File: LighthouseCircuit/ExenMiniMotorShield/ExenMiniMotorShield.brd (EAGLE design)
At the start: 15.2 x 6.3 mm, 13 parts, among them J3 SM02B-SRSS, Q1 DMP2035U

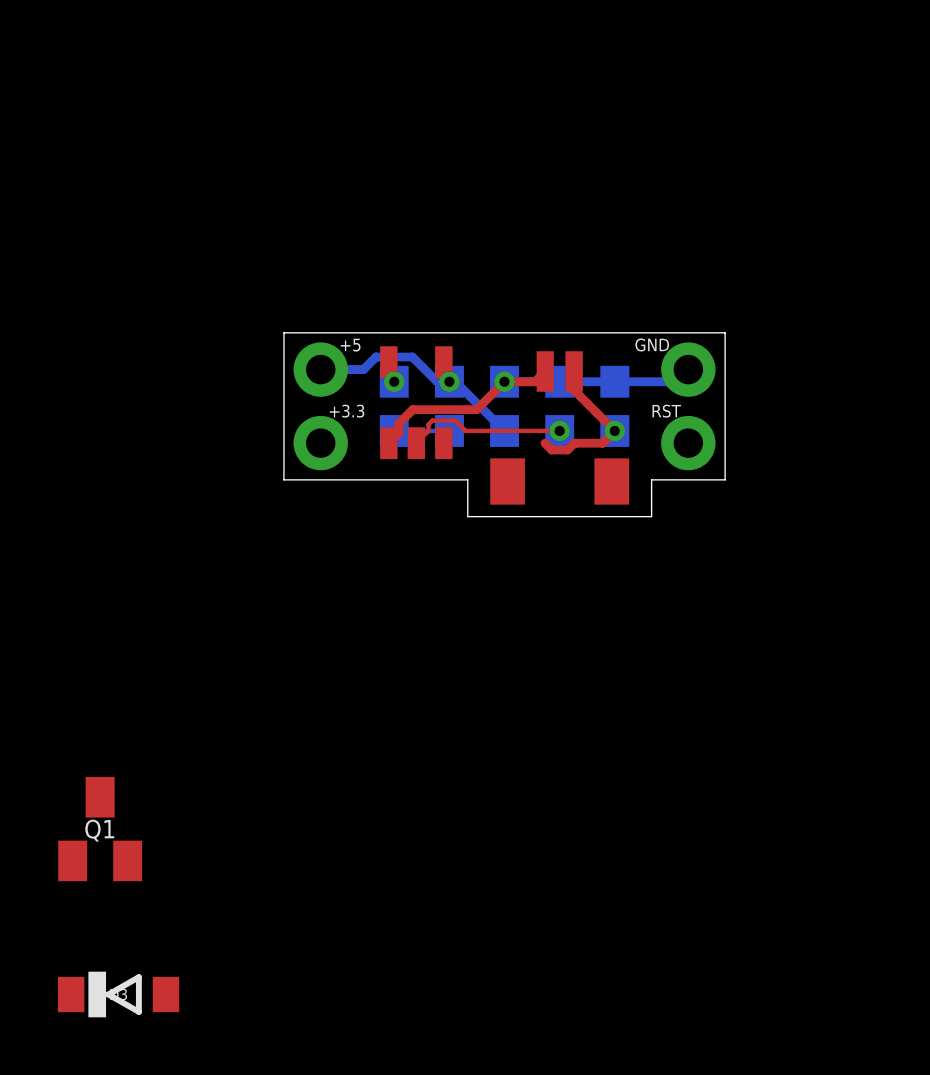
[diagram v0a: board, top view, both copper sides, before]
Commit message: Moved to separate PID configuration for each wheel. Since the left wheel is offset toward the rear and the right wheel is offset toward the front, the left wheel needs to be less aggressive or the Zippy will turn more quickly to the right and will tilt the robot and pull the right wheel off the ground, preventing contact with the floor. On the other hand, the right wheel needs to be more aggressive or turns to the left will be slower than turns to the right.
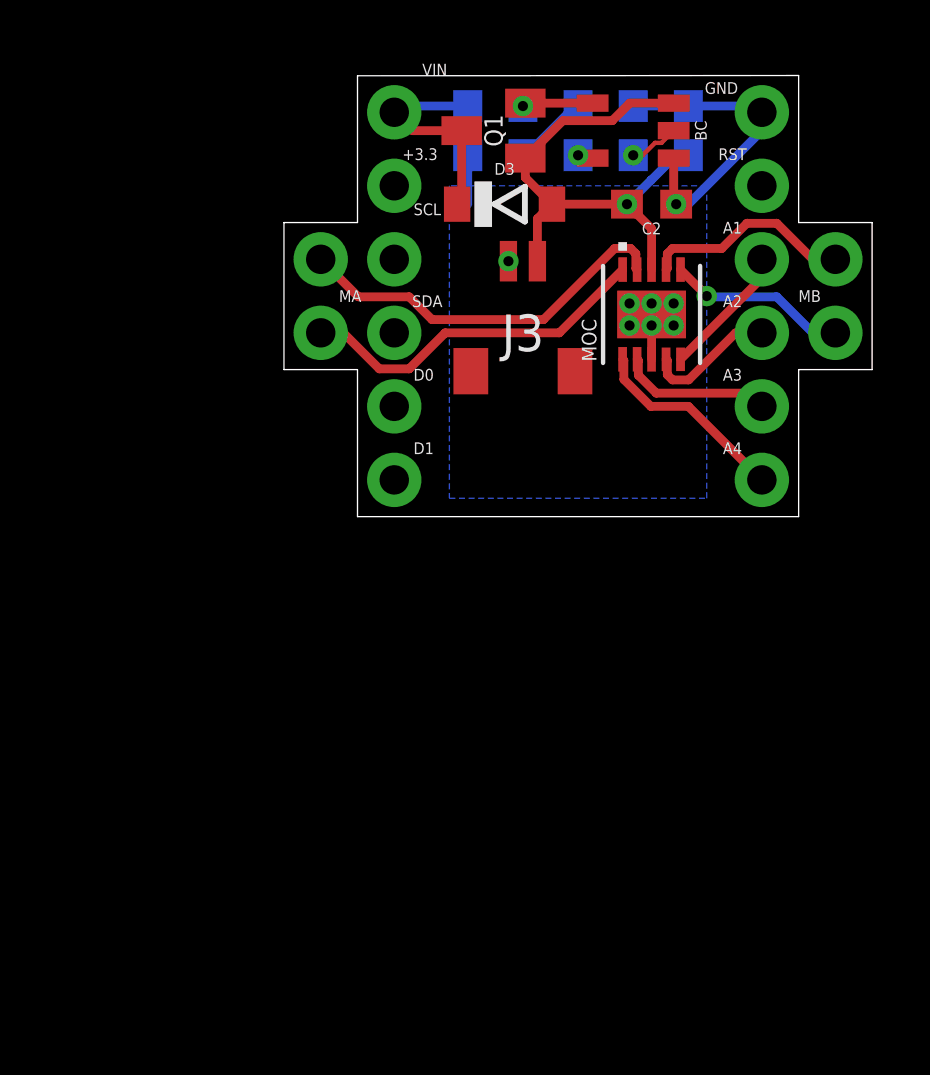
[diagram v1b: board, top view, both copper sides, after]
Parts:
- removed +5: (no value), SparkFun-Connectors:1X01_NO_SILK
- added A1, A2, A3, A4, D0, D1, MA01, MA02, MB01, MBO2, SCL, SDA, VIN: (no value), SparkFun-Connectors:1X01_NO_SILK
- added CB: 10μF, SparkFun-Capacitors:0603
- added MOC: A3901SEJTR-T, ZippyComponentLibrary:DFN-10_DD
- J3: value SM02B-SRSS -> BATTERY
- moved D3 30.4 mm to (7.62, 10.8)
- moved Q1 27.7 mm to (7.24, 13.3), turned to 90 degrees
- moved BC 12.0 mm to (12.1, 13.3), turned to 90 degrees
- moved RBI 11.4 mm to (10.2, 13.3), turned to 270 degrees
- moved DBI 9.86 mm to (8.26, 13.3)
- moved RBO 9.86 mm to (12.1, 13.3)
- moved C1 9.61 mm to (6.35, 13.3), turned to 90 degrees
- moved +3.3 9.25 mm to (3.81, 11.4)
- moved GND 9.25 mm to (16.5, 14.0)
- moved RST 9.25 mm to (16.5, 11.4)
- moved C2 7.10 mm to (12.7, 10.8), flipped to the top, turned to 180 degrees
- moved J3 4.02 mm to (8.26, 6.35)
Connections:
- removed net N$5: BC.VDD, Q1.E
- new net IO1: A1.1, MOC.5
- new net IO2: A2.1, MOC.4
- new net IO3: A3.1, MOC.2
- new net IO4: A4.1, MOC.1
- new net MA01: MBO2.1, MOC.7
- new net MA02: MB01.1, MOC.6
- new net MB01: MA02.1, MOC.10
- new net MB02: MA01.1, MOC.9
- new net VDD: BC.VDD, DBI.1, Q1.E
- net GND: now also CB.1, MOC.11, MOC.3
- net VBAT: now also CB.2, MOC.8, Q1.B
- net VIN: now also VIN.1; no longer +5.1, DBI.1, Q1.B
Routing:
- net MB02: track 0.00 -> 13.4 mm
- net VBAT: track 5.42 -> 18.1 mm
- net MB01: track 0.00 -> 12.4 mm
- net MA01: track 0.00 -> 7.32 mm
- net IO4: track 0.00 -> 6.92 mm
- net MA02: track 0.00 -> 6.26 mm, vias 0 -> 1
- net IO3: track 0.00 -> 5.28 mm
- net IO1: track 0.00 -> 4.62 mm
- net IO2: track 0.00 -> 4.57 mm
- net N$3: track 5.55 -> 1.75 mm
- net VDD: track 0.00 -> 2.46 mm, vias 0 -> 1
- net GND: track 13.1 -> 15.5 mm, vias 1 -> 8
- net N$1: track 1.90 -> 2.61 mm
- net VIN: track 7.86 -> 7.83 mm, vias 1 -> 0
- added copper zone on layer 16, net GND
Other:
- board size 15.2 x 6.3 mm -> 20.3 x 15.2 mm
- board text added: "MA"
- board text added: "MB"

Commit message: Reached a point where auto-drive mode is consistent and reliable.
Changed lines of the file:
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@@
 <layer number="2" name="Route2" color="1" fill="3" visible="no" active="no"/>
 <layer number="15" name="Route15" color="4" fill="6" visible="no" active="no"/>
-<layer number="16" name="Bottom" color="1" fill="1" visible="yes" active="yes"/>
+<layer number="16" name="Bottom" color="1" fill="1" visible="no" active="yes"/>
 <layer number="17" name="Pads" color="2" fill="1" visible="yes" active="yes"/>
 <layer number="18" name="Vias" color="2" fill="1" visible="yes" active="yes"/>
@@
 <layer number="20" name="Dimension" color="15" fill="1" visible="yes" active="yes"/>
 <layer number="21" name="tPlace" color="7" fill="1" visible="yes" active="yes"/>
-<layer number="22" name="bPlace" color="7" fill="1" visible="yes" active="yes"/>
+<layer number="22" name="bPlace" color="7" fill="1" visible="no" active="yes"/>
 <layer number="23" name="tOrigins" color="15" fill="1" visible="yes" active="yes"/>
-<layer number="24" name="bOrigins" color="15" fill="1" visible="yes" active="yes"/>
+<layer number="24" name="bOrigins" color="15" fill="1" visible="no" active="yes"/>
 <layer number="25" name="tNames" color="7" fill="1" visible="yes" active="yes"/>
-<layer number="26" name="bNames" color="7" fill="1" visible="yes" active="yes"/>
-<layer number="27" name="tValues" color="7" fill="1" visible="yes" active="yes"/>
-<layer number="28" name="bValues" color="7" fill="1" visible="yes" active="yes"/>
+<layer number="26" name="bNames" color="7" fill="1" visible="no" active="yes"/>
+<layer number="27" name="tValues" color="7" fill="1" visible="no" active="yes"/>
+<layer number="28" name="bValues" color="7" fill="1" visible="no" active="yes"/>
 <layer number="29" name="tStop" color="7" fill="3" visible="no" active="yes"/>
 <layer number="30" name="bStop" color="7" fill="6" visible="no" active="yes"/>
@@
 <layer number="38" name="bTest" color="7" fill="1" visible="no" active="yes"/>
 <layer number="39" name="tKeepout" color="4" fill="11" visible="yes" active="yes"/>
-<layer number="40" name="bKeepout" color="1" fill="11" visible="yes" active="yes"/>
+<layer number="40" name="bKeepout" color="1" fill="11" visible="no" active="yes"/>
 <layer number="41" name="tRestrict" color="4" fill="10" visible="yes" active="yes"/>
-<layer number="42" name="bRestrict" color="1" fill="10" visible="yes" active="yes"/>
+<layer number="42" name="bRestrict" color="1" fill="10" visible="no" active="yes"/>
 <layer number="43" name="vRestrict" color="2" fill="10" visible="no" active="yes"/>
-<layer number="44" name="Drills" color="7" fill="1" visible="yes" active="yes"/>
+<layer number="44" name="Drills" color="7" fill="1" visible="no" active="yes"/>
 <layer number="45" name="Holes" color="7" fill="1" visible="yes" active="yes"/>
 <layer number="46" name="Milling" color="3" fill="1" visible="no" active="yes"/>
@@
 <layer number="50" name="dxf" color="7" fill="1" visible="no" active="no"/>
 <layer number="51" name="tDocu" color="7" fill="1" visible="yes" active="yes"/>
-<layer number="52" name="bDocu" color="7" fill="1" visible="yes" active="yes"/>
+<layer number="52" name="bDocu" color="7" fill="1" visible="no" active="yes"/>
 <layer number="53" name="tGND_GNDA" color="7" fill="9" visible="no" active="no"/>
 <layer number="54" name="bGND_GNDA" color="1" fill="9" visible="no" active="no"/>
@@
 </element>
 <element name="MOC" library="ZippyComponentLibrary" package="DFN-10_DD" value="A3901SEJTR-T" x="12.7" y="6.985" smashed="yes" rot="R90">
-<attribute name="NAME" x="10.795" y="5.3594" size="0.508" layer="25" font="vector" rot="SR90"/>
+<attribute name="NAME" x="12.7254" y="4.318" size="0.4064" layer="25" font="vector" ratio="7" rot="SR0" align="bottom-center"/>
 </element>
 <element name="A4" library="SparkFun-Connectors" package="1X01_NO_SILK" value="" x="16.51" y="1.27" smashed="yes">
@@
 </element>
 <element name="BC" library="ZippyComponentLibrary" package="SOT-753" value="BATTERYCHARGER" x="12.065" y="13.335" smashed="yes" rot="R90">
-<attribute name="NAME" x="14.605" y="13.335" size="0.4064" layer="25" font="vector" ratio="7" rot="SR90" align="bottom-center"/>
+<attribute name="NAME" x="12.065" y="13.335" size="0.4064" layer="25" font="vector" ratio="7" rot="SR0" align="center"/>
 </element>
 <element name="VIN" library="SparkFun-Connectors" package="1X01_NO_SILK" value="" x="3.81" y="13.97" smashed="yes">
-<attribute name="NAME" x="5.207" y="15.24" size="0.4064" layer="25" font="vector" ratio="7" align="bottom-center"/>
+<attribute name="NAME" x="4.953" y="14.732" size="0.4064" layer="25" font="vector" ratio="7" align="bottom-center"/>
 <attribute name="VALUE" x="2.54" y="12.192" size="0.6096" layer="27" font="vector" ratio="20"/>
 </element>
-<element name="J3" library="tinycircuits" package="JST_SH_2X1" value="BATTERY" x="8.255" y="6.35">
+<element name="J3" library="tinycircuits" package="JST_SH_2X1" value="BATTERY" x="8.255" y="6.35" smashed="yes">
+<attribute name="NAME" x="8.255" y="5.715" size="0.4064" layer="25" font="vector" ratio="7" align="center"/>
 <attribute name="PARTNO" value="AS-ITM-00231" x="-10.795" y="22.225" size="0.3048" layer="27" display="off"/>
 <attribute name="PNPROTATION" value="180" x="-10.795" y="22.225" size="0.3048" layer="27" display="off"/>
 </element>
 <element name="GND" library="SparkFun-Connectors" package="1X01_NO_SILK" value="" x="16.51" y="13.97" smashed="yes">
-<attribute name="NAME" x="15.113" y="14.605" size="0.4064" layer="25" font="vector" ratio="7" align="bottom-center"/>
+<attribute name="NAME" x="15.367" y="14.732" size="0.4064" layer="25" font="vector" ratio="7" align="bottom-center"/>
 <attribute name="VALUE" x="15.24" y="12.192" size="0.6096" layer="27" font="vector" ratio="20"/>
 </element>
@@
 </element>
 <element name="D3" library="tinycircuits" package="SOD-123FL" value="MBR120" x="7.62" y="10.795" smashed="yes">
-<attribute name="NAME" x="7.62" y="11.811" size="0.4064" layer="25" ratio="7" align="bottom-center"/>
+<attribute name="NAME" x="6.985" y="9.525" size="0.4064" layer="25" ratio="7" align="bottom-center"/>
 <attribute name="PARTNO" value="AS-ITM-00111" x="-36.83" y="-40.005" size="0.3048" layer="27" display="off"/>
 </element>
-<element name="Q1" library="tinycircuits" package="SOT23" value="DMP2035U" x="7.239" y="13.335" rot="R90">
+<element name="Q1" library="tinycircuits" package="SOT23" value="DMP2035U" x="7.239" y="13.335" smashed="yes" rot="R90">
+<attribute name="NAME" x="7.366" y="13.335" size="0.4064" layer="25" font="vector" ratio="7" align="center"/>
 <attribute name="PARTNO" value="AS-ITM-00024" x="54.229" y="-31.75" size="0.3048" layer="27" rot="R90" display="off"/>
 <attribute name="PNPROTATION" value="0" x="54.229" y="-31.75" size="0.3048" layer="27" rot="R90" display="off"/>
 </element>
 <element name="SCL" library="SparkFun-Connectors" package="1X01_NO_SILK" value="" x="3.81" y="8.89" smashed="yes">
-<attribute name="NAME" x="4.953" y="10.414" size="0.4064" layer="25" font="vector" ratio="7" align="bottom-center"/>
+<attribute name="NAME" x="4.953" y="9.779" size="0.4064" layer="25" font="vector" ratio="7" align="bottom-center"/>
 <attribute name="VALUE" x="2.54" y="7.112" size="0.6096" layer="27" font="vector" ratio="20"/>
 </element>
@@
 <contactref element="MOC" pad="2"/>
 <contactref element="A3" pad="1"/>
-<wire x1="16.51" y1="3.81" x2="16.0534" y2="4.2666" width="0.3048" layer="1"/>
-<wire x1="12.2428" y1="5.3922" x2="12.2" y2="5.435" width="0.3048" layer="1"/>
-<wire x1="16.0534" y1="4.2666" x2="12.86235" y2="4.2666" width="0.3048" layer="1"/>
-<wire x1="12.86235" y1="4.2666" x2="12.2428" y2="4.88615" width="0.3048" layer="1"/>
-<wire x1="12.2428" y1="4.88615" x2="12.2428" y2="5.3922" width="0.3048" layer="1"/>
+<wire x1="12.2" y1="5.435" x2="12.2428" y2="5.3922" width="0.3048" layer="1"/>
+<wire x1="12.2428" y1="5.3922" x2="12.2428" y2="4.88615" width="0.3048" layer="1"/>
+<wire x1="12.2428" y1="4.88615" x2="13.31895" y2="3.81" width="0.3048" layer="1"/>
+<wire x1="13.31895" y1="3.81" x2="16.51" y2="3.81" width="0.3048" layer="1"/>
 </signal>
 <signal name="IO1">
@@
 <contactref element="MOC" pad="4"/>
 <contactref element="A2" pad="1"/>
-<wire x1="13.97865" y1="4.7238" x2="13.42135" y2="4.7238" width="0.3048" layer="1"/>
-<wire x1="13.42135" y1="4.7238" x2="13.2428" y2="4.90235" width="0.3048" layer="1"/>
-<wire x1="13.2428" y1="4.90235" x2="13.2428" y2="5.3922" width="0.3048" layer="1"/>
+<wire x1="13.97625" y1="4.7052" x2="13.42375" y2="4.7052" width="0.3048" layer="1"/>
 <wire x1="13.2428" y1="5.3922" x2="13.2" y2="5.435" width="0.3048" layer="1"/>
-<wire x1="16.51" y1="6.35" x2="15.60485" y2="6.35" width="0.3048" layer="1"/>
-<wire x1="15.60485" y1="6.35" x2="13.97865" y2="4.7238" width="0.3048" layer="1"/>
+<wire x1="16.51" y1="6.35" x2="15.62105" y2="6.35" width="0.3048" layer="1"/>
+<wire x1="15.62105" y1="6.35" x2="13.97625" y2="4.7052" width="0.3048" layer="1"/>
+<wire x1="13.42375" y1="4.7052" x2="13.2428" y2="4.88615" width="0.3048" layer="1"/>
+<wire x1="13.2428" y1="4.88615" x2="13.2428" y2="5.3922" width="0.3048" layer="1"/>
 </signal>
 <signal name="IO4">
 <contactref element="MOC" pad="1"/>
 <contactref element="A4" pad="1"/>
-<wire x1="16.51" y1="1.27" x2="13.9706" y2="3.8094" width="0.3048" layer="1"/>
-<wire x1="13.9706" y1="3.8094" x2="12.67296875" y2="3.8094" width="0.3048" layer="1"/>
-<wire x1="11.7428" y1="5.3922" x2="11.7" y2="5.435" width="0.3048" layer="1"/>
-<wire x1="12.67296875" y1="3.8094" x2="11.7428" y2="4.73956875" width="0.3048" layer="1"/>
-<wire x1="11.7428" y1="4.73956875" x2="11.7428" y2="5.3922" width="0.3048" layer="1"/>
+<wire x1="11.7" y1="5.435" x2="11.7428" y2="5.3922" width="0.3048" layer="1"/>
+<wire x1="15.21236875" y1="1.27" x2="16.51" y2="1.27" width="0.3048" layer="1"/>
+<wire x1="11.7428" y1="5.3922" x2="11.7428" y2="4.73956875" width="0.3048" layer="1"/>
+<wire x1="11.7428" y1="4.73956875" x2="15.21236875" y2="1.27" width="0.3048" layer="1"/>
 </signal>
 <signal name="N$1">
